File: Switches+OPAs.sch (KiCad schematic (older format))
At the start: 12 parts, among them SW1 SW_Rotary2x6, SW2 SW_Rotary2x6, SW3 SW_Rotary2x6, SW4 SW_Rotary2x6, SW5 SW_Rotary2x6, SW6 SW_Rotary2x6, U1 TL072, U2 TL072, U3 TL072, U4 TL072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

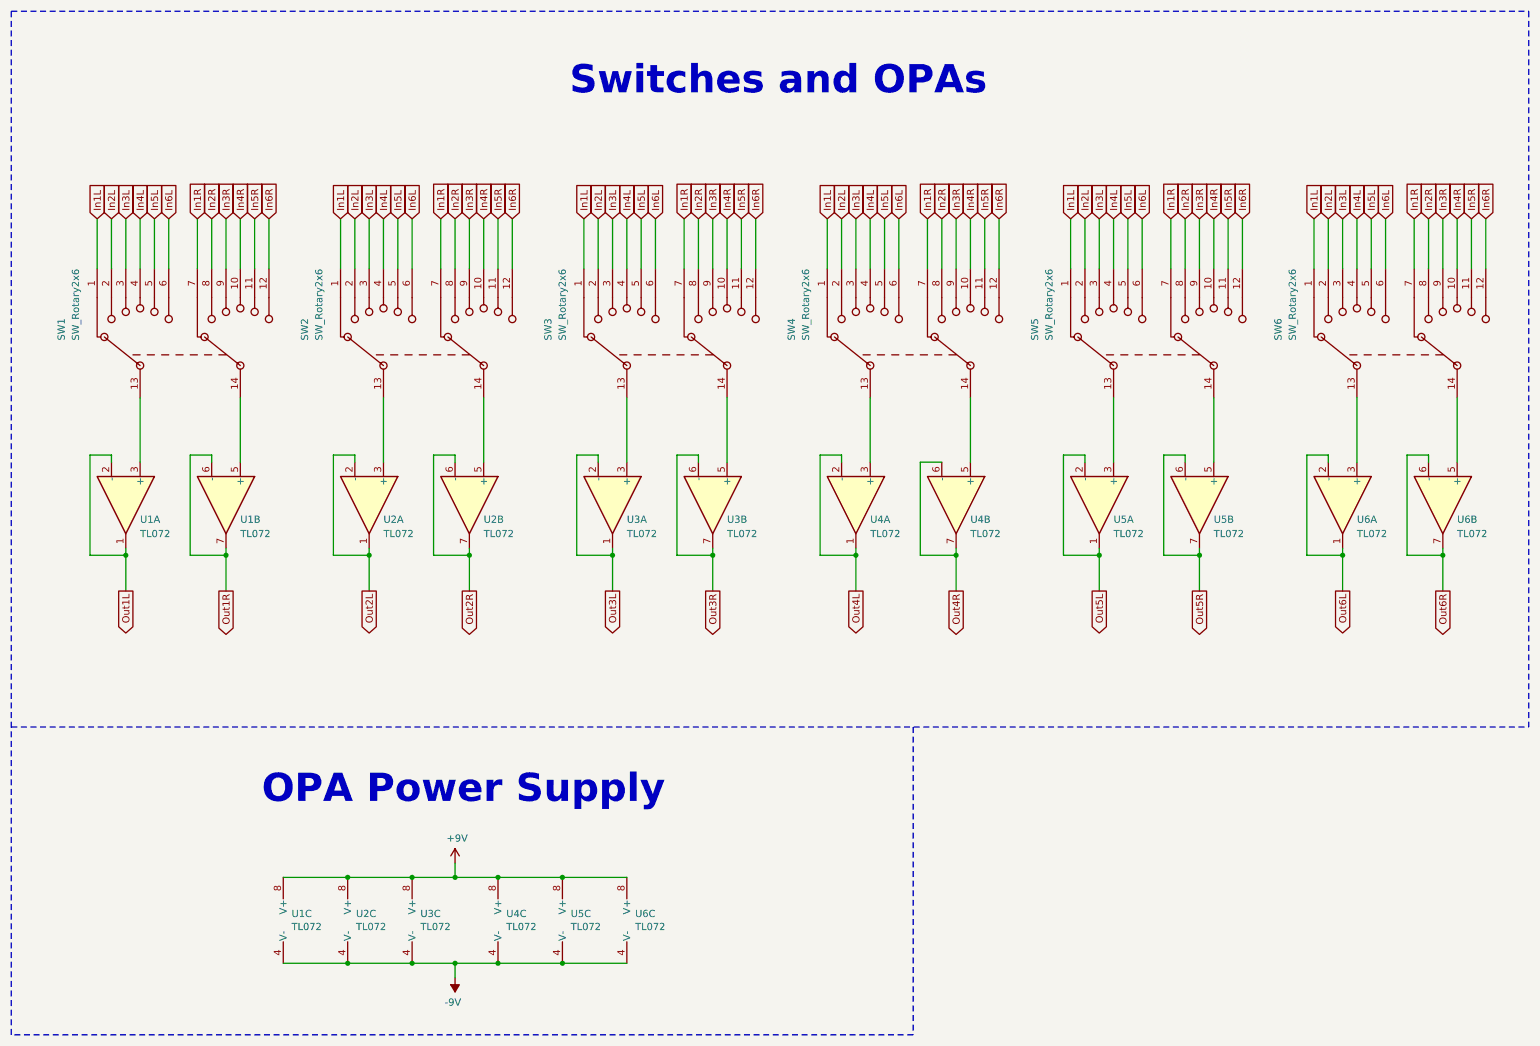
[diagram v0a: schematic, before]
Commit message: added converter for asymmetric power supply | Routing In & Out PCB finished | Routing Switch PCB started
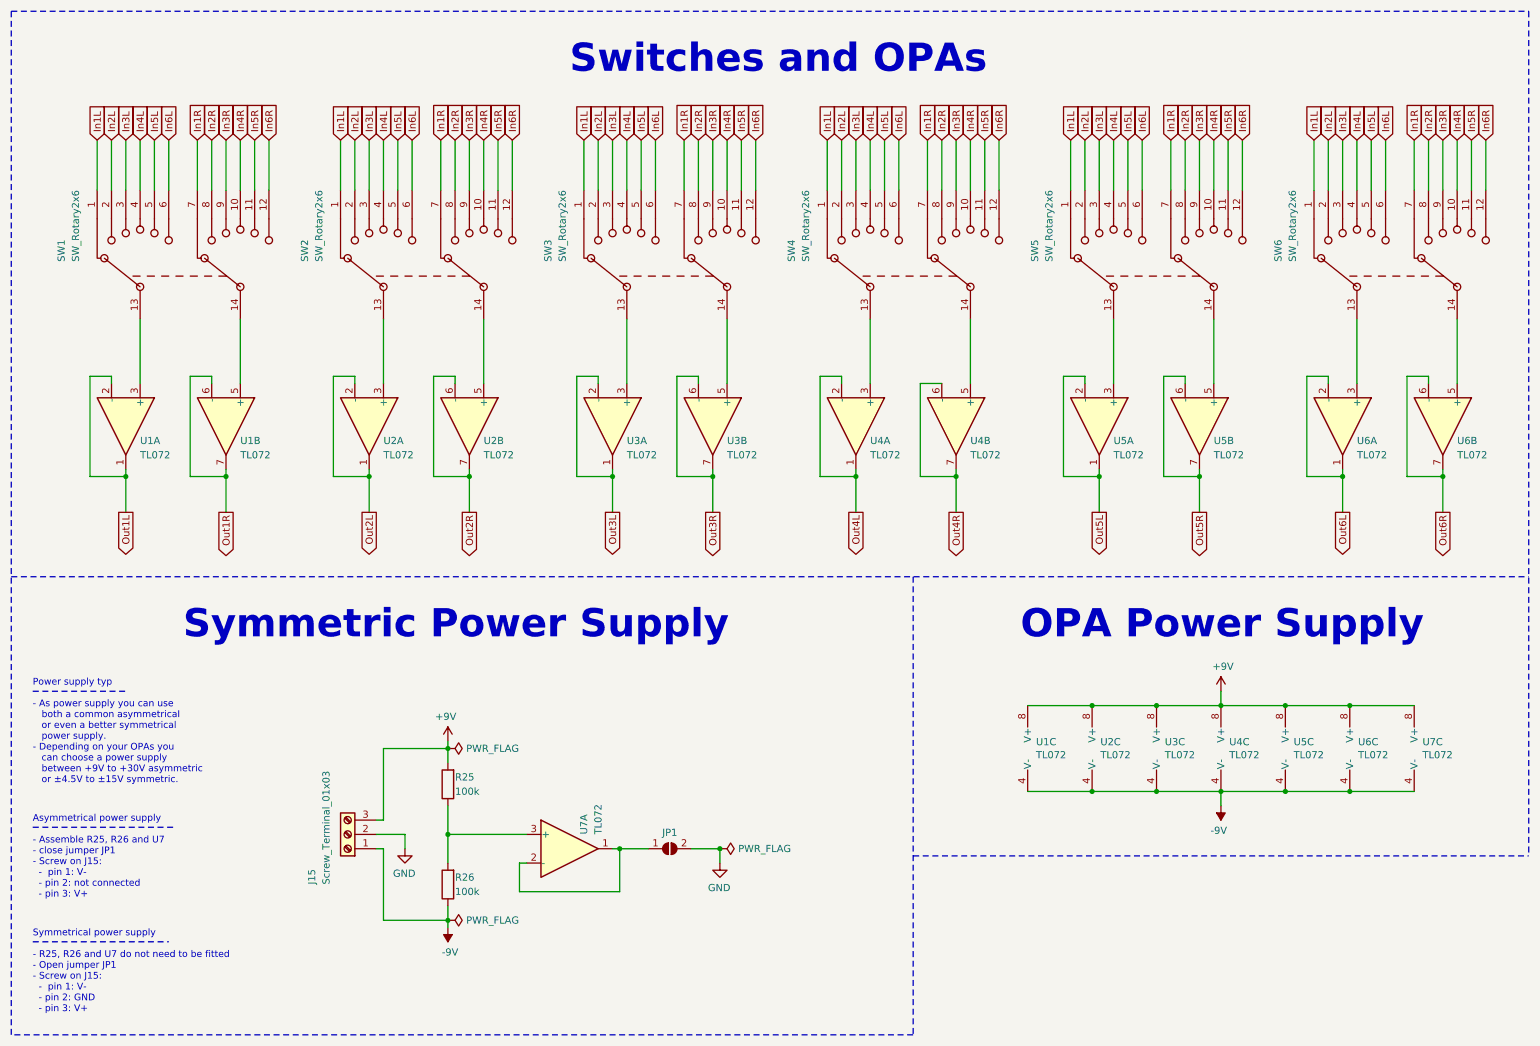
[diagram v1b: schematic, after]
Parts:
- added J15: Screw_Terminal_01x03, h8-Connectors:Wuerth-691102710003, symbol Connector:Screw_Terminal_01x03
- added JP1: SolderJumper_2_Open, Jumper:SolderJumper-2_P1.3mm_Open_TrianglePad1.0x1.5mm, symbol Jumper:SolderJumper_2_Open
- added R25, R26: 100k, Resistor_SMD:R_0603_1608Metric_Pad1.05x0.95mm_HandSolder, symbol Device:R
- added U7: TL072, Package_SO:SOIC-8_3.9x4.9mm_P1.27mm, symbol Amplifier_Operational:TL072
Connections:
- net +9V: now also J15.3 (Pin_3), R25.2, U7.8 (V+)
- net -9V: now also J15.1 (Pin_1), R26.1, U7.4 (V-)
- new net: JP1.1 (A), U7.1, U7.2 (-)
- new net: R25.1, R26.2, U7.3 (+)
- new net GND: J15.2 (Pin_2), JP1.2 (B)
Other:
- note added: "Asymmetrical power supply\n\n- Assemble R25, R26 and U7\n- close jumper JP1\n- Screw on J15: \n - pin 1: V-\n - pin 2: not connected\n - pin 3: V+"
- note added: "Power supply typ\n\n- As power supply you can use \n both a common asymmetrical \n or even a better symmetrical \n power supply. \n- Depending on your OPAs you \n can choose a power supply \n between +9V to +30V asymmetric \n or ±4.5V to ±15V symmetric."
- note added: "Symmetric Power Supply"
- note added: "Symmetrical power supply\n\n- R25, R26 and U7 do not need to be fitted\n- Open jumper JP1 \n- Screw on J15:\n - pin 1: V-\n - pin 2: GND\n - pin 3: V+"
- moved on the sheet: SW1, SW2, SW3, SW4, SW5, SW6, U1A, U1B, U1C, U2A, U2B, U2C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

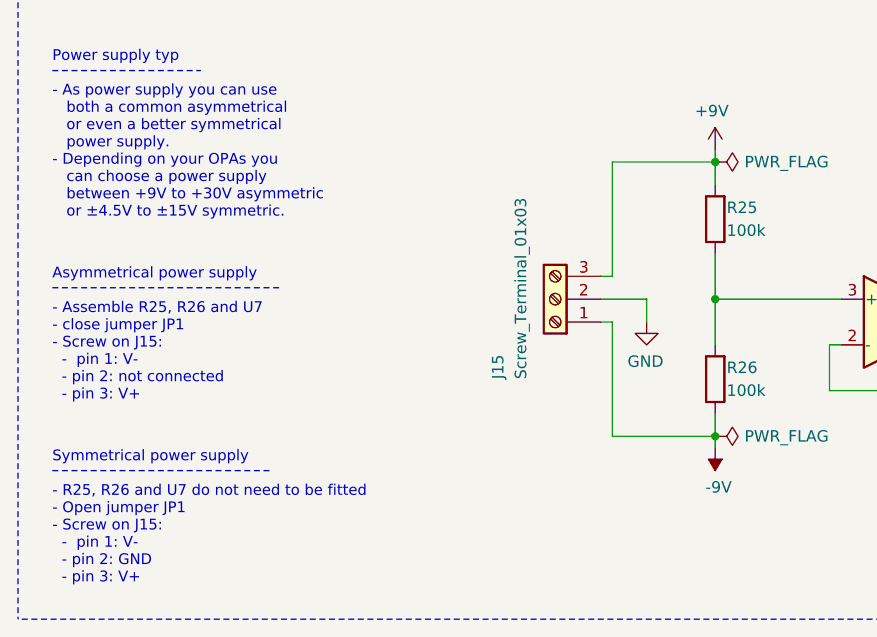
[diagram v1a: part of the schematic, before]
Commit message: swaped supply pins | routing complete → routing revision and optimization necessary
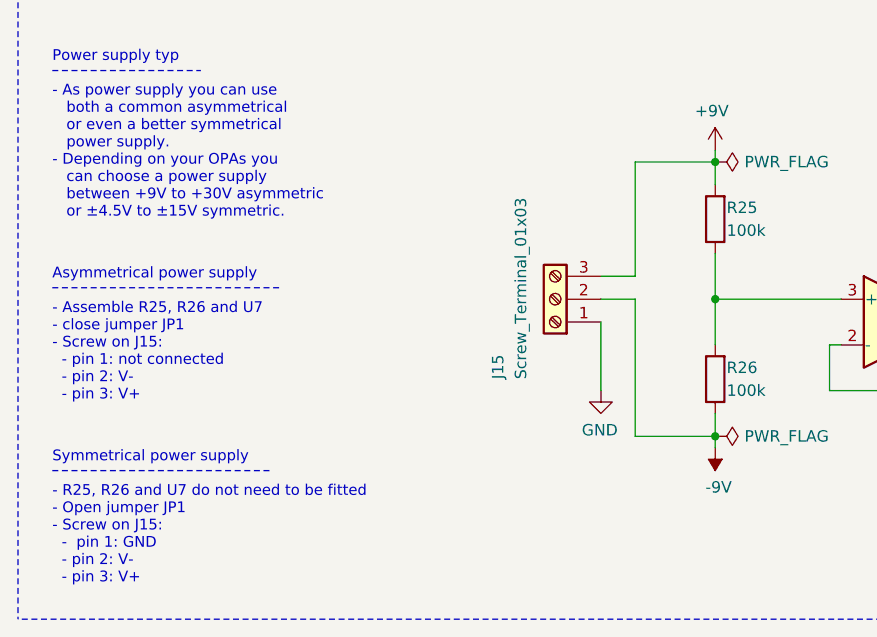
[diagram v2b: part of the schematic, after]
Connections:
- net -9V: now also J15.2 (Pin_2); no longer J15.1 (Pin_1)
- net GND: now also J15.1 (Pin_1); no longer J15.2 (Pin_2)
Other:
- note added: "Asymmetrical power supply\n\n- Assemble R25, R26 and U7\n- close jumper JP1\n- Screw on J15: \n - pin 1: not connected\n - pin 2: V-\n - pin 3: V+"
- note added: "Symmetrical power supply\n\n- R25, R26 and U7 do not need to be fitted\n- Open jumper JP1 \n- Screw on J15:\n - pin 1: GND\n - pin 2: V-\n - pin 3: V+"
- note removed: "Asymmetrical power supply\n\n- Assemble R25, R26 and U7\n- close jumper JP1\n- Screw on J15: \n - pin 1: V-\n - pin 2: not connected\n - pin 3: V+"
- note removed: "Symmetrical power supply\n\n- R25, R26 and U7 do not need to be fitted\n- Open jumper JP1 \n- Screw on J15:\n - pin 1: V-\n - pin 2: GND\n - pin 3: V+"
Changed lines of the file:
@@
 $EndComp
 Wire Wire Line
-	3100 6400 3150 6400
+	3100 6300 3250 6300
 Wire Wire Line
-	3100 6200 3150 6200
+	3100 6200 3250 6200
 Text Notes 1750 4950 0    197  ~ 39
 Symmetric Power Supply
@@
 $EndComp
 Wire Wire Line
-	3150 6400 3150 6900
+	3250 6300 3250 6900
 $Comp
 L Amplifier_Operational:TL072 U7
@@
 Connection ~ 3600 6900
 Wire Wire Line
-	3600 6900 3150 6900
+	3600 6900 3250 6900
 Wire Wire Line
-	3600 5700 3150 5700
+	3600 5700 3250 5700
 Wire Wire Line
-	3150 5700 3150 6200
+	3250 5700 3250 6200
 $Comp
 L power:GND #PWR?
 U 1 1 5ED8AD6B
-P 3300 6400
+P 3100 6700
 AR Path="/5EC982D9/5ED8AD6B" Ref="#PWR?"  Part="1"
 AR Path="/5EC982F4/5ED8AD6B" Ref="#PWR027"  Part="1"
-F 0 "#PWR027" H 3300 6150 50  0001 C CNN
-F 1 "GND" H 3305 6227 50  0000 C CNN
-F 2 "" H 3300 6400 50  0001 C CNN
-F 3 "" H 3300 6400 50  0001 C CNN
-	1    3300 6400
+F 0 "#PWR027" H 3100 6450 50  0001 C CNN
+F 1 "GND" H 3105 6527 50  0000 C CNN
+F 2 "" H 3100 6700 50  0001 C CNN
+F 3 "" H 3100 6700 50  0001 C CNN
+	1    3100 6700
 	-1   0    0    -1
 $EndComp
-Wire Wire Line
-	3100 6300 3300 6300
-Wire Wire Line
-	3300 6400 3300 6300
 Text Notes 700  7550 0    47   ~ 0
-Symmetrical power supply\n\n- R25, R26 and U7 do not need to be fitted\n- Open jumper JP1 \n- Screw on J15:\n  -  pin 1: V-\n  - pin 2: GND\n  - pin 3: V+
+Symmetrical power supply\n\n- R25, R26 and U7 do not need to be fitted\n- Open jumper JP1 \n- Screw on J15:\n  -  pin 1: GND\n  - pin 2: V-\n  - pin 3: V+
 $Comp
 L Jumper:SolderJumper_2_Open JP1
@@
 	5300 6400 5500 6400
 Text Notes 700  6750 0    47   ~ 0
-Asymmetrical power supply\n\n- Assemble R25, R26 and U7\n- close jumper JP1\n- Screw on J15: \n  -  pin 1: V-\n  - pin 2: not connected\n  - pin 3: V+
+Asymmetrical power supply\n\n- Assemble R25, R26 and U7\n- close jumper JP1\n- Screw on J15: \n  - pin 1: not connected\n  - pin 2: V-\n  - pin 3: V+
 Text Notes 700  5950 0    47   ~ 0
 Power supply typ\n\n- As power supply you can use \n   both a common asymmetrical \n   or even a better symmetrical \n   power supply. \n- Depending on your OPAs you \n   can choose a power supply \n   between +9V to +30V asymmetric \n   or ±4.5V to ±15V symmetric.
@@
 Wire Wire Line
 	8550 6000 9000 6000
+Wire Wire Line
+	3100 6400 3100 6700
 $EndSCHEMATC

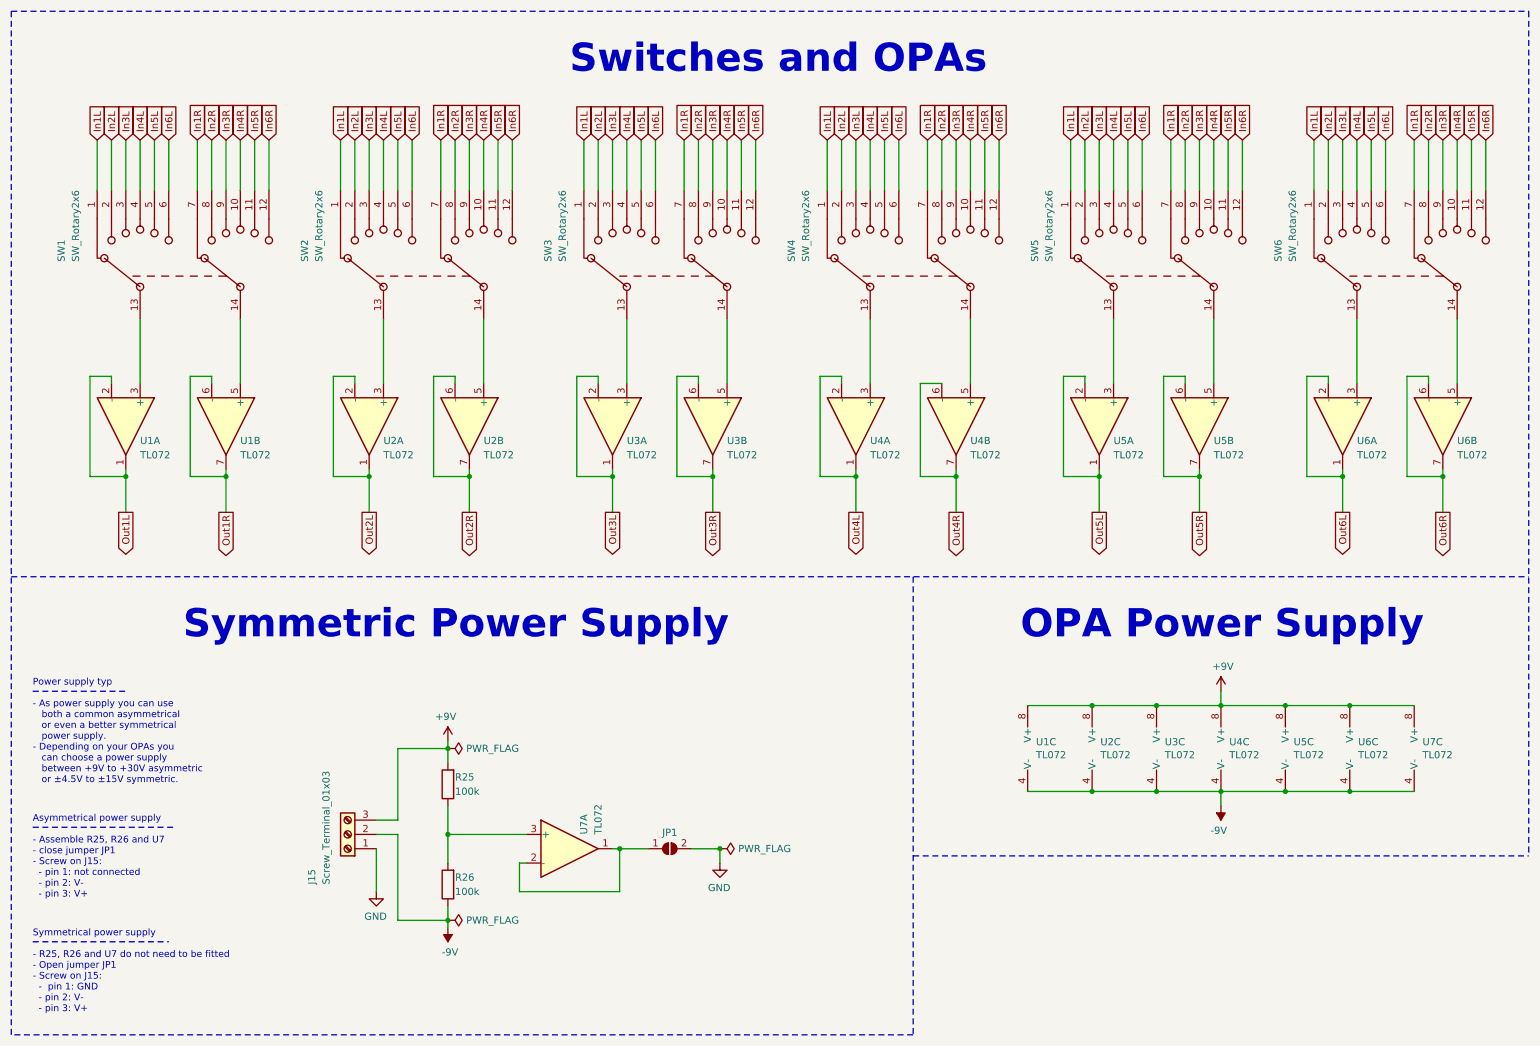
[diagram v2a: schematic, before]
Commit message: finished routing | added GND polygon | added description in surface plot  | added pictures to README.md documentation | changed LICENCE.md to CC BY 4.0
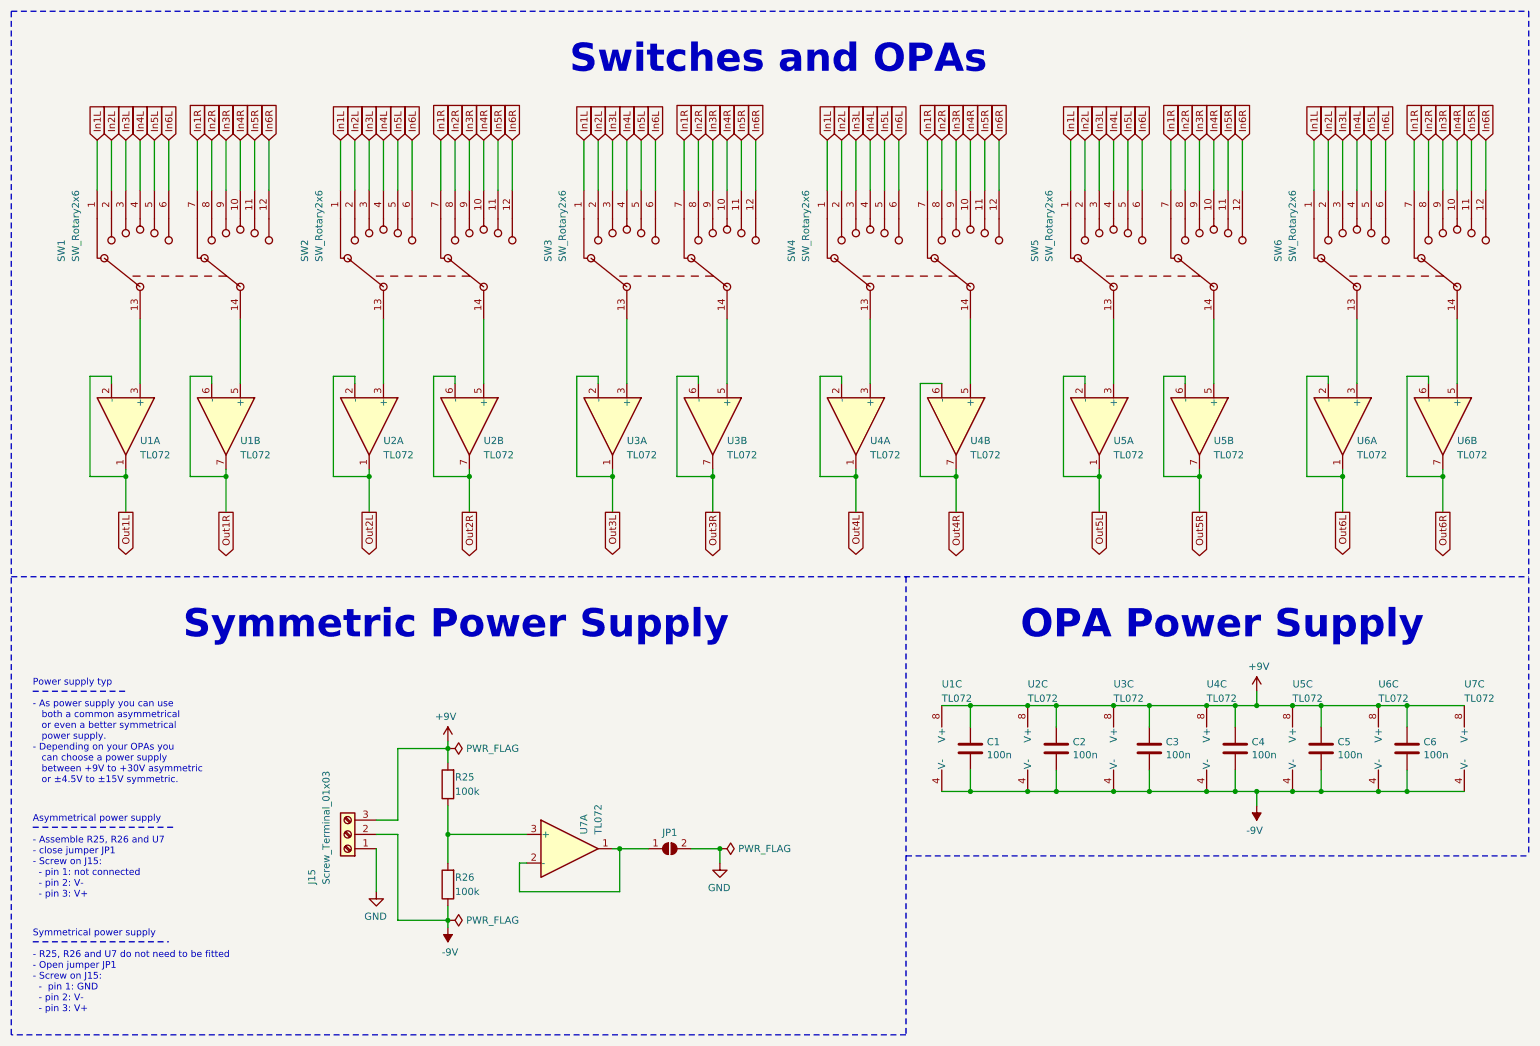
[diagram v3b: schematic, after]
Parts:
- added C1, C2, C3, C4, C5, C6: 100n, Capacitor_SMD:C_0603_1608Metric_Pad1.05x0.95mm_HandSolder, symbol Device:C
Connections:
- net +9V: now also C1.1, C2.1, C3.1, C4.1, C5.1, C6.1
- net -9V: now also C1.2, C2.2, C3.2, C4.2, C5.2, C6.2
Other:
- moved on the sheet: U1C, U2C, U3C, U4C, U5C, U6C, U7C
